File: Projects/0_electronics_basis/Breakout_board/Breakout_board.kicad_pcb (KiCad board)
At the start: 2 copper layers, 26.7 x 27.9 mm, 31 parts, among them J1 DF11-8DP-2DS(24), J2 DF11-8DP-2DS(24), J3 Header11Contacts, U1 ST3485ECDR, U2 TPS5401

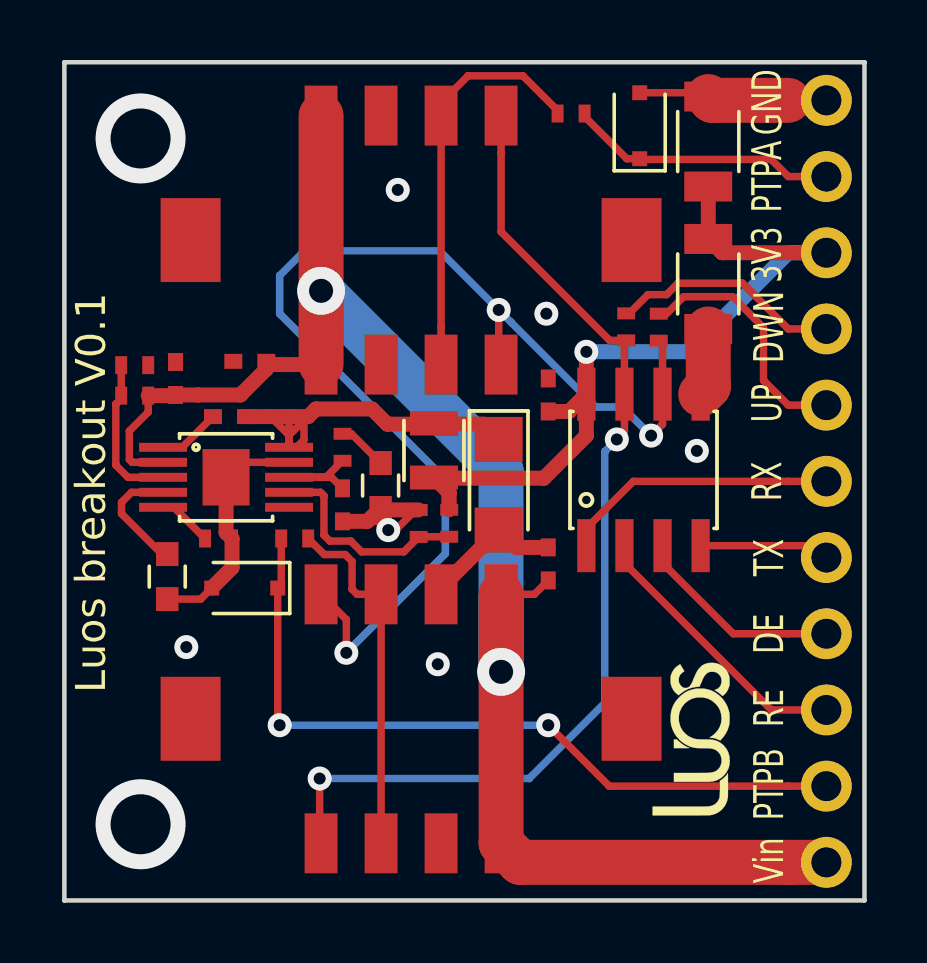
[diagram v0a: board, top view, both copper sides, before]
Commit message: change board kicad for project : Braekout board Luos Kit DC motor Servo
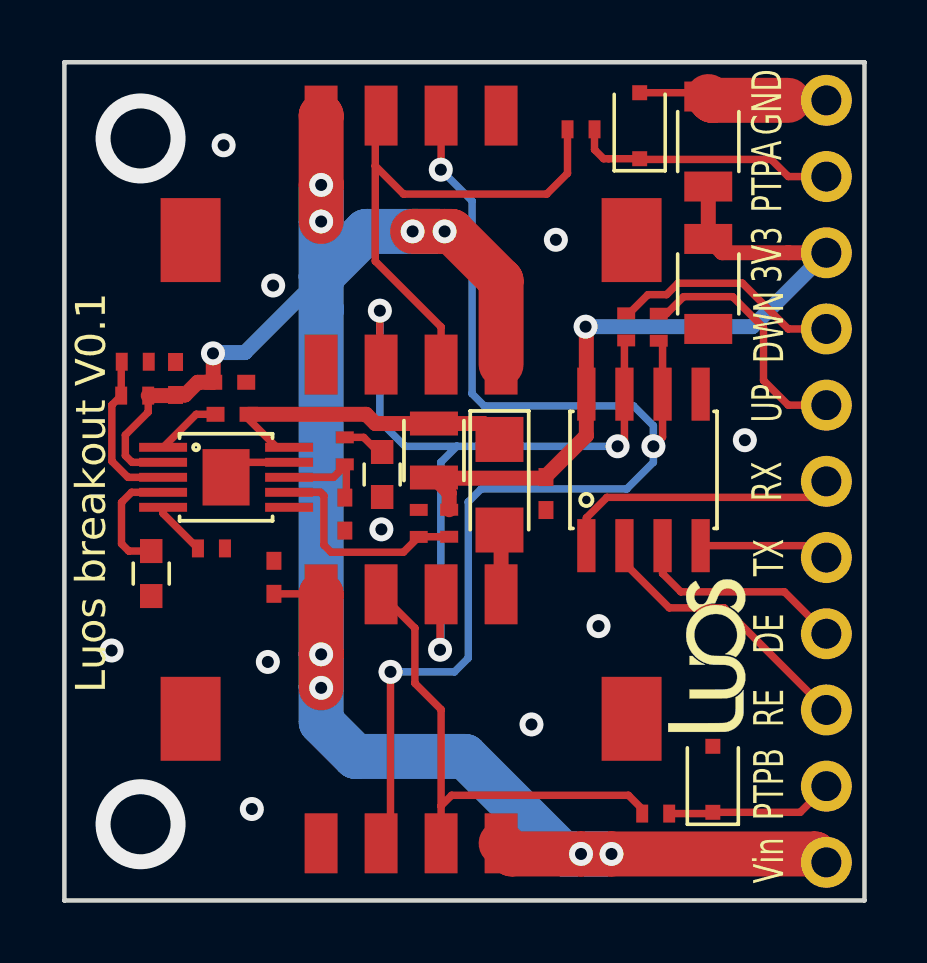
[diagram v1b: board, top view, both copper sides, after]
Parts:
- moved D2 16.9 mm to (85.9, 52.0), turned to 90 degrees
- moved R1 15.1 mm to (84.0, 53.1), turned to 180 degrees
- moved C2 9.15 mm to (71.2, 45.2)
- moved C7 3.29 mm to (80.3, 42.4), turned to 270 degrees
- moved G*** 2.83 mm to (85.7, 47.7)
- moved C3 0.97 mm to (69.8, 38.7), turned to 0 degrees
- moved R2 0.62 mm to (81.5, 30.3)
- moved C6 0.54 mm to (67.2, 45.1)
- moved R8 0.41 mm to (69.2, 44.3)
- moved C5 0.37 mm to (74.9, 41.8)
- moved C4 0.32 mm to (73.6, 43.1)
- moved R5 0.14 mm to (73.6, 41.0)
- moved R4 0.12 mm to (66.6, 38.0)
- moved C8 0.11 mm to (69.8, 39.8)
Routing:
- net /PTPB: track 25.4 -> 5.62 mm, vias 2 -> 0
- net GND: track 26.8 -> 9.54 mm, vias 6 -> 10
- net /Vin: track 54.7 -> 71.8 mm, vias 2 -> 9
- net /B_RS_485_P: track 34.7 -> 26.5 mm, vias 2 -> 3
- net /PTPA_PRO: track 13.6 -> 17.8 mm
- net /PTPB_PRO: track 12.0 -> 16.2 mm
- net /A_RS_485_N: track 39.0 -> 41.9 mm
- net Net-(C8-Pad1): track 13.4 -> 10.8 mm
- net +3V3: track 26.8 -> 25.8 mm
- net Net-(C4-Pad1): track 3.94 -> 3.20 mm
